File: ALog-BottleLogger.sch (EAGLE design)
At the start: 102 parts, among them IC2 ATMEGA644M, Q1 220mA/50V/3.5Ω, Q11 220mA/50V/3.5Ω, Q12 4.3A/20V/54mΩ, Q5 4.3A/20V/54mΩ, Q6 4.3A/20V/54mΩ, Q7 4.3A/20V/54mΩ, Q8 220mA/50V/3.5Ω, Q9 220mA/50V/3.5Ω, U2 FT231X-Q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

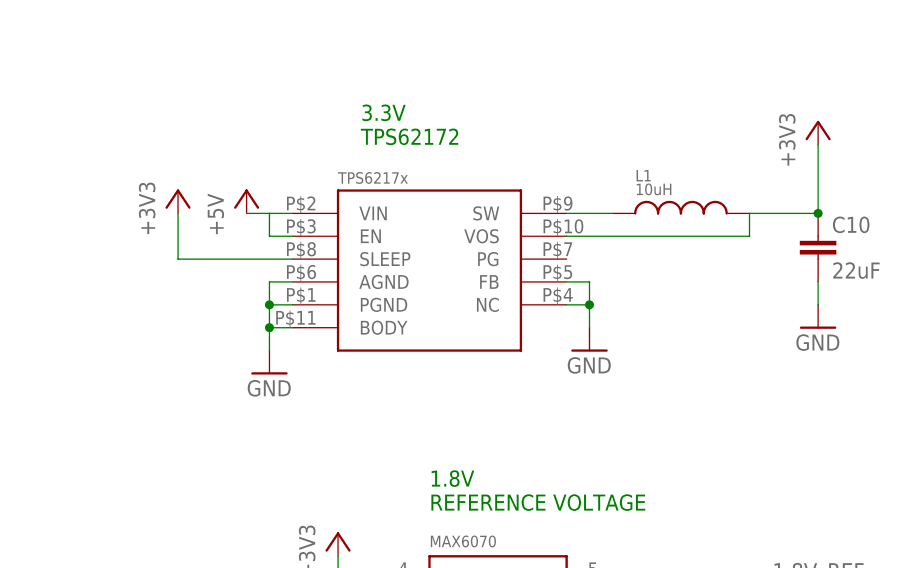
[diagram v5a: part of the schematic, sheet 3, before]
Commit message: Changed 3.3 voltage regulator to TPS62172
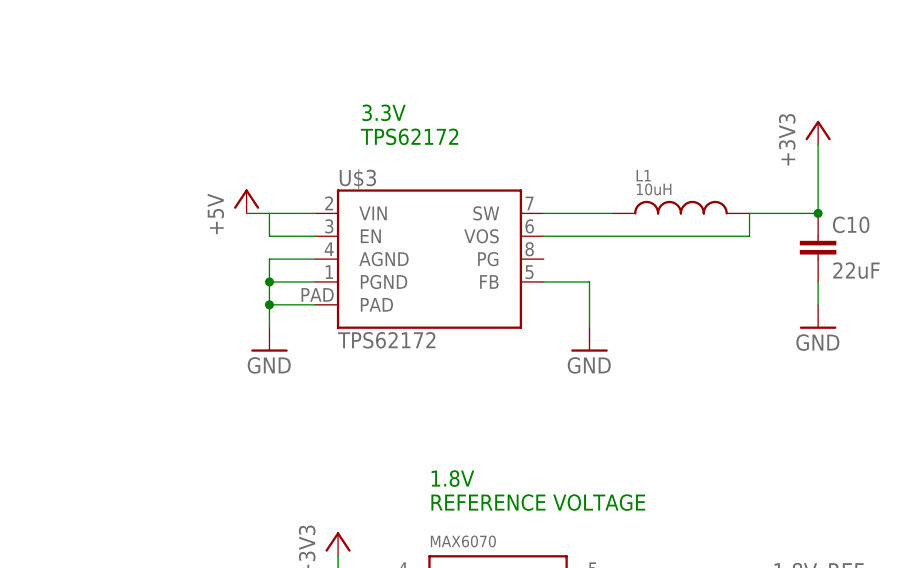
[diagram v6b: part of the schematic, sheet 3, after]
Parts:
- U$3: value TPS6217X -> TPS62172; device texas:TPS6217X -> SparkFun-IC-Power:TPS62172
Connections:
- net +3V3: no longer U$3.SLEEP
- net GND: now also U$3.PAD; no longer U$3.BODY, U$3.NC
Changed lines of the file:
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@@
 <part name="C1" library="rcl" deviceset="C-EU" device="C0805" value="22uF"/>
 <part name="C2" library="rcl" deviceset="C-EU" device="C0805" value="22uF"/>
-<part name="U$3" library="texas" deviceset="TPS6217X" device=""/>
+<part name="U$3" library="SparkFun-IC-Power" deviceset="TPS62172" device=""/>
 <part name="GND2" library="supply1" deviceset="GND" device=""/>
 <part name="GND3" library="supply1" deviceset="GND" device=""/>
@@
 <part name="+3V3" library="supply1" deviceset="+3V3" device=""/>
 <part name="+3V4" library="supply1" deviceset="+3V3" device=""/>
-<part name="+3V5" library="supply1" deviceset="+3V3" device=""/>
 <part name="+3V7" library="supply1" deviceset="+3V3" device=""/>
 <part name="+3V8" library="supply1" deviceset="+3V3" device=""/>
@@
 <instance part="C1" gate="G$1" x="-10.16" y="104.14"/>
 <instance part="C2" gate="G$1" x="-25.4" y="104.14"/>
-<instance part="U$3" gate="G$1" x="-63.5" y="48.26"/>
+<instance part="U$3" gate="G$1" x="-63.5" y="50.8"/>
 <instance part="GND2" gate="1" x="-45.72" y="40.64"/>
-<instance part="GND3" gate="1" x="-81.28" y="38.1"/>
+<instance part="GND3" gate="1" x="-81.28" y="40.64"/>
 <instance part="L1" gate="G$1" x="-35.56" y="55.88"/>
 <instance part="GND16" gate="1" x="-20.32" y="43.18"/>
 <instance part="C10" gate="G$1" x="-20.32" y="53.34"/>
 <instance part="+3V4" gate="G$1" x="-20.32" y="66.04"/>
-<instance part="+3V5" gate="G$1" x="-91.44" y="58.42"/>
 <instance part="P+2" gate="1" x="0" y="111.76"/>
 <instance part="P+3" gate="1" x="-83.82" y="58.42"/>
@@
 </segment>
 <segment>
+<pinref part="GND3" gate="1" pin="GND"/>
+<wire x1="-81.28" y1="50.8" x2="-81.28" y2="48.26" width="0.1524" layer="91"/>
+<pinref part="U$3" gate="G$1" pin="PGND"/>
+<wire x1="-81.28" y1="48.26" x2="-81.28" y2="45.72" width="0.1524" layer="91"/>
+<wire x1="-81.28" y1="45.72" x2="-81.28" y2="43.18" width="0.1524" layer="91"/>
+<wire x1="-76.2" y1="48.26" x2="-81.28" y2="48.26" width="0.1524" layer="91"/>
+<junction x="-81.28" y="48.26"/>
 <pinref part="U$3" gate="G$1" pin="AGND"/>
-<wire x1="-78.74" y1="48.26" x2="-81.28" y2="48.26" width="0.1524" layer="91"/>
-<pinref part="GND3" gate="1" pin="GND"/>
-<wire x1="-81.28" y1="48.26" x2="-81.28" y2="45.72" width="0.1524" layer="91"/>
-<pinref part="U$3" gate="G$1" pin="PGND"/>
-<wire x1="-81.28" y1="45.72" x2="-81.28" y2="43.18" width="0.1524" layer="91"/>
-<wire x1="-81.28" y1="43.18" x2="-81.28" y2="40.64" width="0.1524" layer="91"/>
-<pinref part="U$3" gate="G$1" pin="BODY"/>
-<wire x1="-78.74" y1="43.18" x2="-81.28" y2="43.18" width="0.1524" layer="91"/>
-<junction x="-81.28" y="43.18"/>
-<wire x1="-78.74" y1="45.72" x2="-81.28" y2="45.72" width="0.1524" layer="91"/>
+<wire x1="-81.28" y1="50.8" x2="-76.2" y2="50.8" width="0.1524" layer="91"/>
+<pinref part="U$3" gate="G$1" pin="PAD"/>
+<wire x1="-81.28" y1="45.72" x2="-76.2" y2="45.72" width="0.1524" layer="91"/>
 <junction x="-81.28" y="45.72"/>
 </segment>
 <segment>
-<pinref part="U$3" gate="G$1" pin="NC"/>
-<wire x1="-45.72" y1="45.72" x2="-45.72" y2="48.26" width="0.1524" layer="91"/>
 <pinref part="U$3" gate="G$1" pin="FB"/>
-<wire x1="-45.72" y1="48.26" x2="-48.26" y2="48.26" width="0.1524" layer="91"/>
-<wire x1="-48.26" y1="45.72" x2="-45.72" y2="45.72" width="0.1524" layer="91"/>
+<wire x1="-45.72" y1="48.26" x2="-50.8" y2="48.26" width="0.1524" layer="91"/>
 <pinref part="GND2" gate="1" pin="GND"/>
-<wire x1="-45.72" y1="45.72" x2="-45.72" y2="43.18" width="0.1524" layer="91"/>
-<junction x="-45.72" y="45.72"/>
+<wire x1="-45.72" y1="48.26" x2="-45.72" y2="43.18" width="0.1524" layer="91"/>
 </segment>
 <segment>
@@
 <pinref part="U$3" gate="G$1" pin="SW"/>
 <pinref part="L1" gate="G$1" pin="P$1"/>
-<wire x1="-48.26" y1="55.88" x2="-43.18" y2="55.88" width="0.1524" layer="91"/>
+<wire x1="-50.8" y1="55.88" x2="-43.18" y2="55.88" width="0.1524" layer="91"/>
 </segment>
 </net>
 <net name="+3V3" class="0">
-<segment>
-<pinref part="+3V5" gate="G$1" pin="+3V3"/>
-<pinref part="U$3" gate="G$1" pin="SLEEP"/>
-<wire x1="-78.74" y1="50.8" x2="-91.44" y2="50.8" width="0.1524" layer="91"/>
-<wire x1="-91.44" y1="50.8" x2="-91.44" y2="55.88" width="0.1524" layer="91"/>
-</segment>
 <segment>
 <pinref part="U$3" gate="G$1" pin="VOS"/>
@@
 <wire x1="-20.32" y1="55.88" x2="-27.94" y2="55.88" width="0.1524" layer="91"/>
 <wire x1="-27.94" y1="55.88" x2="-27.94" y2="53.34" width="0.1524" layer="91"/>
-<wire x1="-27.94" y1="53.34" x2="-48.26" y2="53.34" width="0.1524" layer="91"/>
+<wire x1="-27.94" y1="53.34" x2="-50.8" y2="53.34" width="0.1524" layer="91"/>
 <pinref part="C10" gate="G$1" pin="1"/>
 <pinref part="+3V4" gate="G$1" pin="+3V3"/>
@@
 <segment>
 <pinref part="U$3" gate="G$1" pin="EN"/>
-<wire x1="-78.74" y1="53.34" x2="-81.28" y2="53.34" width="0.1524" layer="91"/>
+<wire x1="-76.2" y1="53.34" x2="-81.28" y2="53.34" width="0.1524" layer="91"/>
 <wire x1="-81.28" y1="53.34" x2="-81.28" y2="55.88" width="0.1524" layer="91"/>
 <pinref part="U$3" gate="G$1" pin="VIN"/>
-<wire x1="-81.28" y1="55.88" x2="-78.74" y2="55.88" width="0.1524" layer="91"/>
+<wire x1="-81.28" y1="55.88" x2="-76.2" y2="55.88" width="0.1524" layer="91"/>
 <wire x1="-83.82" y1="55.88" x2="-81.28" y2="55.88" width="0.1524" layer="91"/>
 <pinref part="P+3" gate="1" pin="+5V"/>

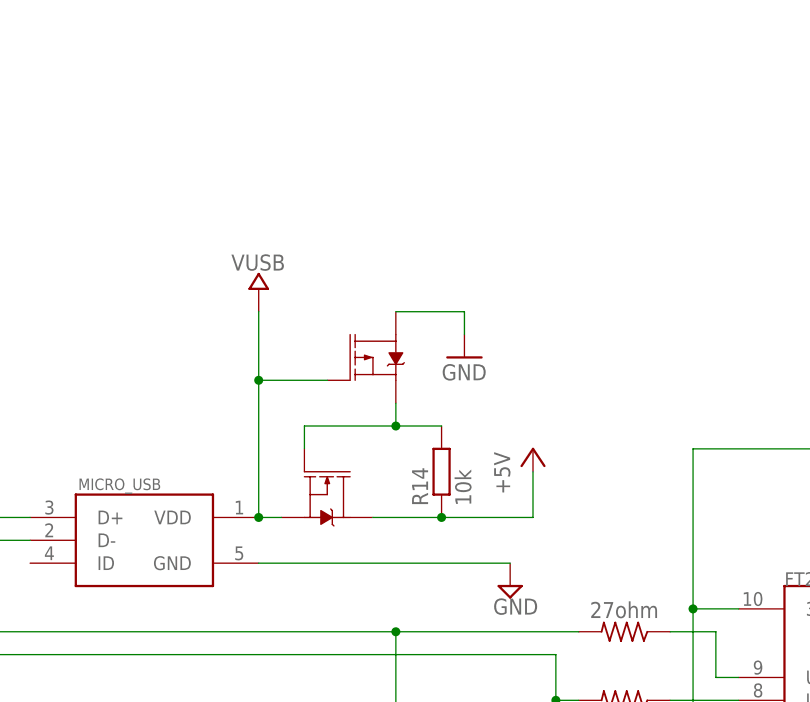
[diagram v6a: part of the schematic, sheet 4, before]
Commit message: Fixed USB FTDI mosphet connections, updated 3.3V regulator, fixed ground connection on 1.8V reg
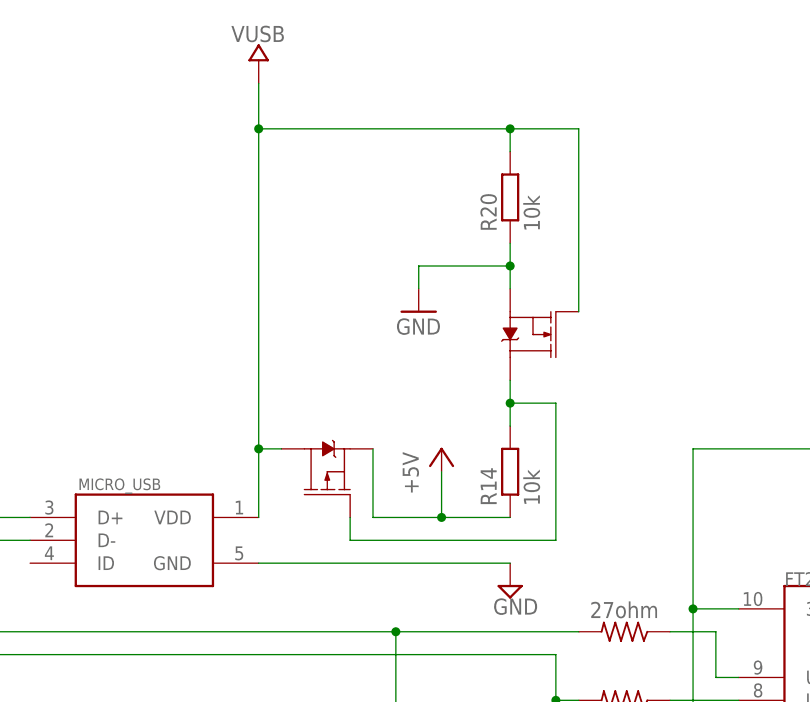
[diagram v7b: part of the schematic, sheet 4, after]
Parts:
- removed L1: 10uH, Custom:WE-LSQ(INDUCTOR)
- added R20: 10k, rcl:R-EU_R0603
- added U$6: 74404020022, csandell:74404020022
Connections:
- removed net N$9: U$2.GND
- net +3V3: now also U$6.2; no longer L1.P$2
- net +5V: now also Q12.S; no longer Q11.D
- net GND: now also Q11.S, R20.1, U$2.GND; no longer Q12.D
- net N$1: now also U$6.1; no longer L1.P$1
- net N$11: now also Q11.D, Q12.G; no longer Q11.G, Q12.S
- net VUSB: now also Q11.G, Q12.D, R20.2; no longer Q11.S, Q12.G
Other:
- moved on the sheet: R14
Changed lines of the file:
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@@
 <part name="GND2" library="supply1" deviceset="GND" device=""/>
 <part name="GND3" library="supply1" deviceset="GND" device=""/>
-<part name="L1" library="Custom" deviceset="WE-LSQ(INDUCTOR)" device="" value="10uH"/>
 <part name="GND16" library="supply1" deviceset="GND" device=""/>
 <part name="C10" library="rcl" deviceset="C-EU" device="C0805" value="22uF"/>
@@
 <part name="U3" library="microbuilder" deviceset="VREG_TPS63060/1" device="" value="TPS63060"/>
 <part name="GND33" library="SparkFun-PowerSymbols" deviceset="GND" device=""/>
+<part name="R20" library="rcl" deviceset="R-EU_" device="R0603" value="10k"/>
+<part name="U$6" library="csandell" deviceset="74404020022" device=""/>
 </parts>
 <sheets>
@@
 <instance part="GND2" gate="1" x="-45.72" y="40.64"/>
 <instance part="GND3" gate="1" x="-81.28" y="40.64"/>
-<instance part="L1" gate="G$1" x="-35.56" y="55.88"/>
 <instance part="GND16" gate="1" x="-20.32" y="43.18"/>
 <instance part="C10" gate="G$1" x="-20.32" y="53.34"/>
@@
 <instance part="U3" gate="G$1" x="-66.04" y="101.6"/>
 <instance part="GND33" gate="1" x="-50.8" y="83.82"/>
+<instance part="U$6" gate="G$1" x="-35.56" y="55.88" smashed="yes" rot="R90">
+<attribute name="NAME" x="-35.56" y="62.23" size="1.778" layer="95" rot="R180"/>
+<attribute name="VALUE" x="-30.48" y="59.69" size="1.778" layer="96" rot="R180"/>
+</instance>
 </instances>
 <busses>
@@
 </segment>
 <segment>
-<wire x1="-40.64" y1="5.08" x2="-40.64" y2="2.54" width="0.1524" layer="91"/>
-<pinref part="GND5" gate="1" pin="GND"/>
-</segment>
-<segment>
 <wire x1="-104.14" y1="7.62" x2="-104.14" y2="5.08" width="0.1524" layer="91"/>
 <pinref part="GND6" gate="1" pin="GND"/>
@@
 <wire x1="-53.34" y1="93.98" x2="-50.8" y2="93.98" width="0.1524" layer="91"/>
 <wire x1="-50.8" y1="93.98" x2="-50.8" y2="86.36" width="0.1524" layer="91"/>
+</segment>
+<segment>
+<pinref part="U$2" gate="G$1" pin="GND"/>
+<wire x1="-43.18" y1="5.08" x2="-40.64" y2="5.08" width="0.1524" layer="91"/>
+<pinref part="GND5" gate="1" pin="GND"/>
+<wire x1="-40.64" y1="5.08" x2="-40.64" y2="2.54" width="0.1524" layer="91"/>
 </segment>
 </net>
@@
 <segment>
 <pinref part="U$3" gate="G$1" pin="SW"/>
-<pinref part="L1" gate="G$1" pin="P$1"/>
 <wire x1="-50.8" y1="55.88" x2="-43.18" y2="55.88" width="0.1524" layer="91"/>
+<pinref part="U$6" gate="G$1" pin="1"/>
 </segment>
 </net>
@@
 <segment>
 <pinref part="U$3" gate="G$1" pin="VOS"/>
-<pinref part="L1" gate="G$1" pin="P$2"/>
 <wire x1="-20.32" y1="55.88" x2="-27.94" y2="55.88" width="0.1524" layer="91"/>
 <wire x1="-27.94" y1="55.88" x2="-27.94" y2="53.34" width="0.1524" layer="91"/>
-<wire x1="-27.94" y1="53.34" x2="-50.8" y2="53.34" width="0.1524" layer="91"/>
 <pinref part="C10" gate="G$1" pin="1"/>
 <pinref part="+3V4" gate="G$1" pin="+3V3"/>
+<wire x1="-27.94" y1="53.34" x2="-50.8" y2="53.34" width="0.1524" layer="91"/>
 <wire x1="-20.32" y1="55.88" x2="-20.32" y2="63.5" width="0.1524" layer="91"/>
 <junction x="-20.32" y="55.88"/>
+<pinref part="U$6" gate="G$1" pin="2"/>
+<junction x="-27.94" y="55.88"/>
 </segment>
 <segment>
@@
 <wire x1="-83.82" y1="55.88" x2="-81.28" y2="55.88" width="0.1524" layer="91"/>
 <pinref part="P+3" gate="1" pin="+5V"/>
-</segment>
-</net>
-<net name="N$9" class="0">
-<segment>
-<pinref part="U$2" gate="G$1" pin="GND"/>
-<wire x1="-43.18" y1="5.08" x2="-40.64" y2="5.08" width="0.1524" layer="91"/>
 </segment>
 </net>
@@
 </instance>
 <instance part="U$8" gate="G$1" x="86.36" y="106.68"/>
-<instance part="U$10" gate="G$1" x="15.24" y="129.54"/>
-<instance part="P+10" gate="1" x="45.72" y="111.76"/>
-<instance part="Q11" gate="NMOS" x="22.86" y="106.68" smashed="yes" rot="R270"/>
-<instance part="Q12" gate="G$1" x="27.94" y="121.92" smashed="yes"/>
-<instance part="R14" gate="G$1" x="35.56" y="109.22" rot="R90"/>
-<instance part="GND21" gate="1" x="38.1" y="121.92"/>
+<instance part="U$10" gate="G$1" x="15.24" y="154.94"/>
+<instance part="P+10" gate="1" x="35.56" y="111.76"/>
+<instance part="Q11" gate="NMOS" x="45.72" y="124.46" smashed="yes" rot="R180"/>
+<instance part="Q12" gate="G$1" x="22.86" y="109.22" smashed="yes" rot="R90"/>
+<instance part="R14" gate="G$1" x="43.18" y="109.22" rot="R90"/>
+<instance part="GND21" gate="1" x="33.02" y="127"/>
+<instance part="R20" gate="G$1" x="43.18" y="139.7" rot="R90"/>
 </instances>
 <busses>
@@
 <segment>
 <pinref part="U$10" gate="G$1" pin="VUSB"/>
-<wire x1="15.24" y1="104.14" x2="15.24" y2="119.38" width="0.1524" layer="91"/>
+<wire x1="15.24" y1="104.14" x2="15.24" y2="111.76" width="0.1524" layer="91"/>
 <pinref part="MICRO_USB" gate="G$1" pin="VDD"/>
-<wire x1="15.24" y1="119.38" x2="15.24" y2="127" width="0.1524" layer="91"/>
-<wire x1="17.78" y1="104.14" x2="15.24" y2="104.14" width="0.1524" layer="91"/>
-<junction x="15.24" y="104.14"/>
-<pinref part="Q11" gate="NMOS" pin="S"/>
-<pinref part="Q12" gate="G$1" pin="G"/>
-<wire x1="22.86" y1="119.38" x2="15.24" y2="119.38" width="0.1524" layer="91"/>
-<junction x="15.24" y="119.38"/>
+<pinref part="Q12" gate="G$1" pin="D"/>
+<wire x1="15.24" y1="111.76" x2="15.24" y2="147.32" width="0.1524" layer="91"/>
+<wire x1="15.24" y1="147.32" x2="15.24" y2="152.4" width="0.1524" layer="91"/>
+<wire x1="15.24" y1="111.76" x2="17.78" y2="111.76" width="0.1524" layer="91"/>
+<junction x="15.24" y="111.76"/>
+<pinref part="Q11" gate="NMOS" pin="G"/>
+<wire x1="50.8" y1="127" x2="50.8" y2="147.32" width="0.1524" layer="91"/>
+<wire x1="50.8" y1="147.32" x2="43.18" y2="147.32" width="0.1524" layer="91"/>
+<junction x="15.24" y="147.32"/>
+<pinref part="R20" gate="G$1" pin="2"/>
+<wire x1="43.18" y1="147.32" x2="15.24" y2="147.32" width="0.1524" layer="91"/>
+<wire x1="43.18" y1="147.32" x2="43.18" y2="144.78" width="0.1524" layer="91"/>
+<junction x="43.18" y="147.32"/>
 </segment>
 </net>
@@
 <segment>
 <pinref part="GND21" gate="1" pin="GND"/>
-<pinref part="Q12" gate="G$1" pin="D"/>
-<wire x1="38.1" y1="127" x2="38.1" y2="124.46" width="0.1524" layer="91"/>
-<wire x1="30.48" y1="127" x2="38.1" y2="127" width="0.1524" layer="91"/>
+<wire x1="33.02" y1="132.08" x2="33.02" y2="129.54" width="0.1524" layer="91"/>
+<pinref part="Q11" gate="NMOS" pin="S"/>
+<pinref part="R20" gate="G$1" pin="1"/>
+<wire x1="43.18" y1="129.54" x2="43.18" y2="132.08" width="0.1524" layer="91"/>
+<wire x1="43.18" y1="132.08" x2="43.18" y2="134.62" width="0.1524" layer="91"/>
+<wire x1="43.18" y1="132.08" x2="33.02" y2="132.08" width="0.1524" layer="91"/>
+<junction x="43.18" y="132.08"/>
 </segment>
 </net>
@@
 </segment>
 </net>
+<net name="+5V" class="0">
+<segment>
+<pinref part="R14" gate="G$1" pin="1"/>
+<wire x1="43.18" y1="104.14" x2="35.56" y2="104.14" width="0.1524" layer="91"/>
+<pinref part="Q12" gate="G$1" pin="S"/>
+<wire x1="35.56" y1="104.14" x2="27.94" y2="104.14" width="0.1524" layer="91"/>
+<wire x1="27.94" y1="111.76" x2="27.94" y2="104.14" width="0.1524" layer="91"/>
+<pinref part="P+10" gate="1" pin="+5V"/>
+<wire x1="35.56" y1="109.22" x2="35.56" y2="104.14" width="0.1524" layer="91"/>
+<junction x="35.56" y="104.14"/>
+</segment>
+</net>
 <net name="N$11" class="0">
 <segment>
-<pinref part="Q11" gate="NMOS" pin="G"/>
-<pinref part="Q12" gate="G$1" pin="S"/>
-<wire x1="20.32" y1="111.76" x2="20.32" y2="114.3" width="0.1524" layer="91"/>
-<wire x1="20.32" y1="114.3" x2="30.48" y2="114.3" width="0.1524" layer="91"/>
+<pinref part="Q12" gate="G$1" pin="G"/>
+<wire x1="25.4" y1="104.14" x2="25.4" y2="101.6" width="0.1524" layer="91"/>
+<wire x1="25.4" y1="101.6" x2="48.26" y2="101.6" width="0.1524" layer="91"/>
+<wire x1="48.26" y1="101.6" x2="48.26" y2="116.84" width="0.1524" layer="91"/>
+<wire x1="48.26" y1="116.84" x2="43.18" y2="116.84" width="0.1524" layer="91"/>
+<pinref part="Q11" gate="NMOS" pin="D"/>
+<wire x1="43.18" y1="116.84" x2="43.18" y2="119.38" width="0.1524" layer="91"/>
 <pinref part="R14" gate="G$1" pin="2"/>
-<wire x1="30.48" y1="114.3" x2="30.48" y2="116.84" width="0.1524" layer="91"/>
-<wire x1="35.56" y1="114.3" x2="30.48" y2="114.3" width="0.1524" layer="91"/>
-<junction x="30.48" y="114.3"/>
-</segment>
-</net>
-<net name="+5V" class="0">
-<segment>
-<pinref part="Q11" gate="NMOS" pin="D"/>
-<pinref part="R14" gate="G$1" pin="1"/>
-<wire x1="27.94" y1="104.14" x2="35.56" y2="104.14" width="0.1524" layer="91"/>
-<wire x1="35.56" y1="104.14" x2="45.72" y2="104.14" width="0.1524" layer="91"/>
-<wire x1="45.72" y1="104.14" x2="45.72" y2="109.22" width="0.1524" layer="91"/>
-<junction x="35.56" y="104.14"/>
-<pinref part="P+10" gate="1" pin="+5V"/>
-</segment>
-</net>
+<wire x1="43.18" y1="116.84" x2="43.18" y2="114.3" width="0.1524" layer="91"/>
+<junction x="43.18" y="116.84"/>
+</segment>
+</net>
